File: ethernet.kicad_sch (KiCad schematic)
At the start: 38 parts

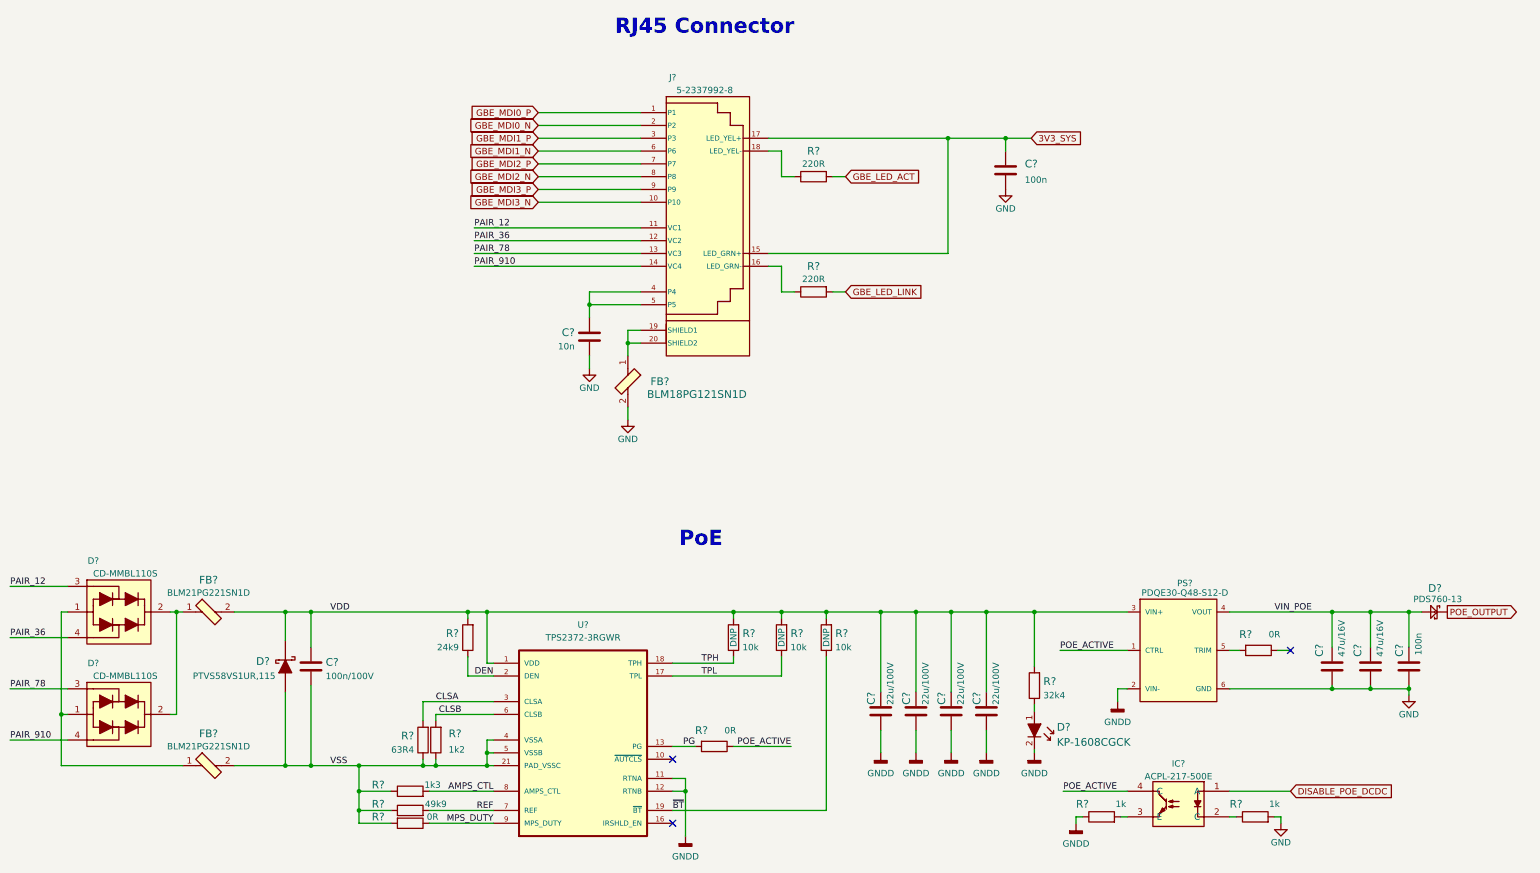
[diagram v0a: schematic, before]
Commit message: Added soft power button and annotated schematic
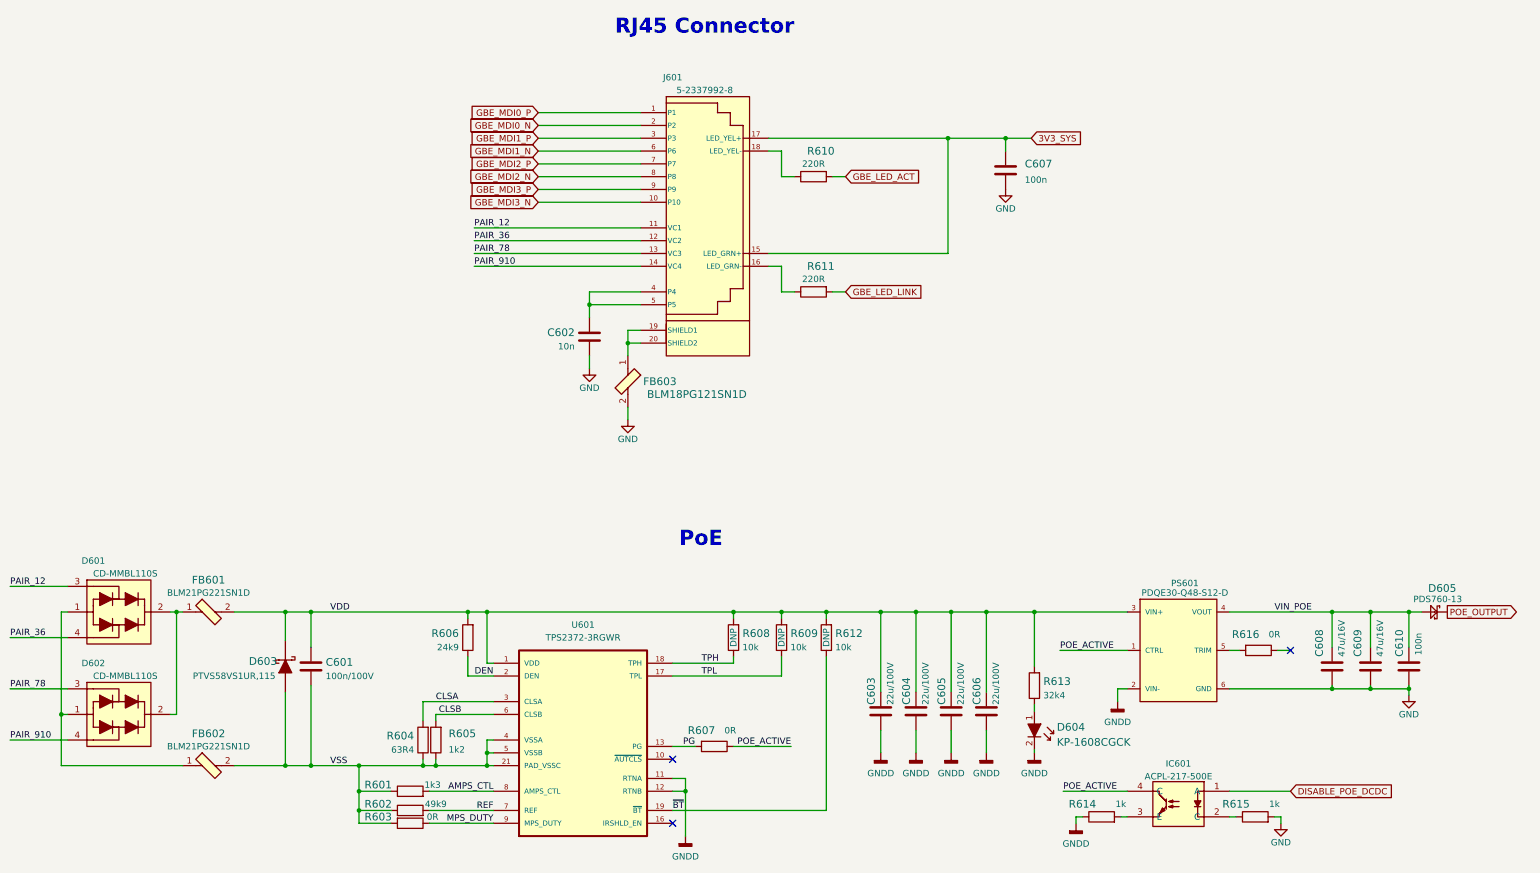
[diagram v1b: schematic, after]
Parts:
- gave numbers to parts that had none: 38

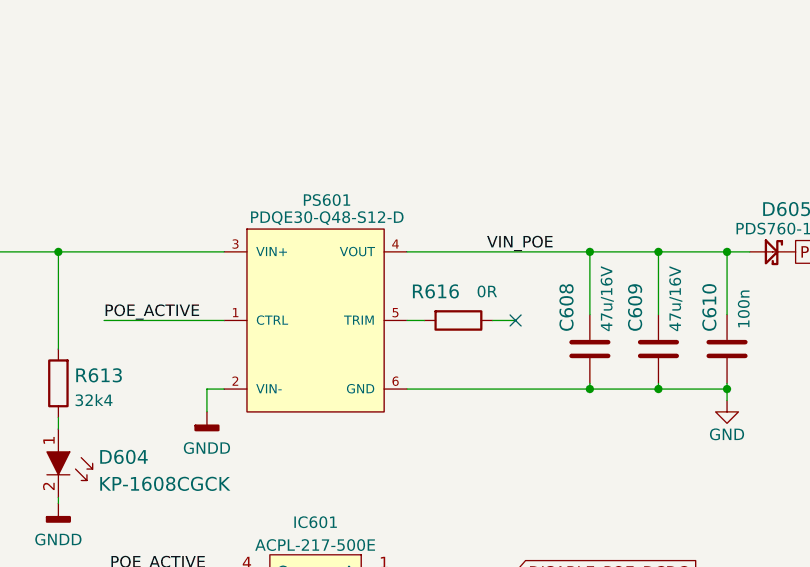
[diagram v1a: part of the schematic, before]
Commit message: Change PoE isolated DCDC to ULS-12/5-D48N-C
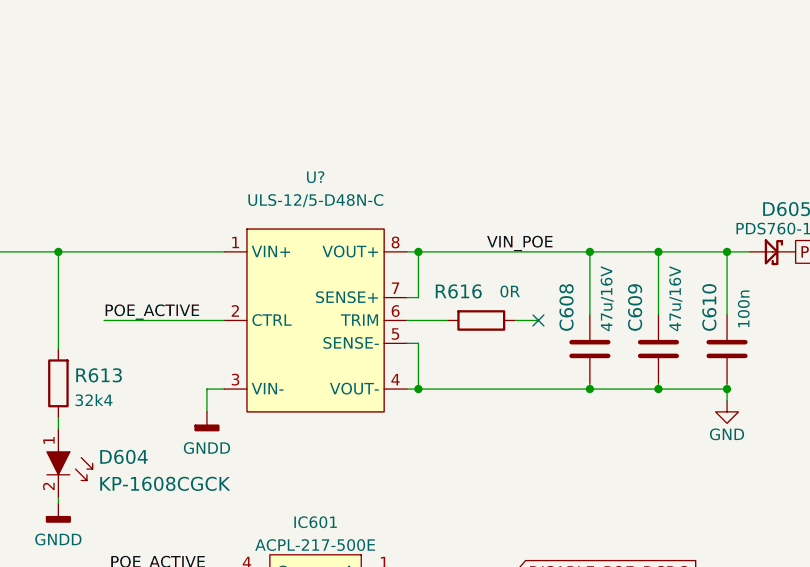
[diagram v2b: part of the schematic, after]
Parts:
- removed PS601: PDQE30-Q48-S12-D, antmicro-footprints:PDQE30-Q48, symbol antmicroDCDCConverters:PDQE30-Q48-S12-D
- added U?: ULS-12/5-D48N-C, antmicro-footprints:ULS-12_5-D48N-C, symbol antmicroDCDCConverters:ULS-12{brace}slash}5-D48N-C
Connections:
- net GND: now also U?.4 (VOUT-), U?.5 (SENSE-)
- net GNDD: now also U?.3 (VIN-)
- net POE_ACTIVE: now also U?.2 (CTRL)
- net VDD: now also U?.1 (VIN+)
- net VIN_POE: now also U?.7 (SENSE+), U?.8 (VOUT+)
- net at R616.2: now also U?.6 (TRIM)
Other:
- moved on the sheet: R616
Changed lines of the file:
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@@
   (junction (at 210.82 177.8) (diameter 0) (color 0 0 0 0)
   )
+  (junction (at 300.99 193.04) (diameter 0) (color 0 0 0 0)
+  )
   (junction (at 112.395 208.28) (diameter 0) (color 0 0 0 0)
   )
@@
   (junction (at 67.945 198.12) (diameter 0) (color 0 0 0 0)
   )
+  (junction (at 300.99 177.8) (diameter 0) (color 0 0 0 0)
+  )
   (junction (at 255.27 83.82) (diameter 0) (color 0 0 0 0)
   )
@@
   (no_connect (at 189.23 207.01))
   (no_connect (at 189.23 219.71))
-  (no_connect (at 311.785 185.42))
+  (no_connect (at 314.325 185.42))
   (wire (pts (xy 208.28 83.82) (xy 243.84 83.82))
     (stroke (width 0) (type default) (color 0 0 0 0))
   )
+  (wire (pts (xy 300.99 187.96) (xy 300.99 193.04))
+    (stroke (width 0) (type default) (color 0 0 0 0))
+  )
   (wire (pts (xy 210.82 86.36) (xy 208.28 86.36))
     (stroke (width 0) (type default) (color 0 0 0 0))
@@
     (stroke (width 0) (type default) (color 0 0 0 0))
   )
-  (wire (pts (xy 299.72 177.8) (xy 320.04 177.8))
+  (wire (pts (xy 299.72 177.8) (xy 300.99 177.8))
     (stroke (width 0) (type default) (color 0 0 0 0))
   )
@@
     (stroke (width 0) (type default) (color 0 0 0 0))
   )
+  (wire (pts (xy 299.72 182.88) (xy 300.99 182.88))
+    (stroke (width 0) (type default) (color 0 0 0 0))
+  )
   (wire (pts (xy 67.945 198.12) (xy 67.945 208.28))
     (stroke (width 0) (type default) (color 0 0 0 0))
@@
     (stroke (width 0) (type default) (color 0 0 0 0))
   )
+  (wire (pts (xy 300.99 182.88) (xy 300.99 177.8))
+    (stroke (width 0) (type default) (color 0 0 0 0))
+  )
   (wire (pts (xy 237.49 205.74) (xy 237.49 201.295))
     (stroke (width 0) (type default) (color 0 0 0 0))
@@
     (stroke (width 0) (type default) (color 0 0 0 0))
   )
+  (wire (pts (xy 300.99 193.04) (xy 320.04 193.04))
+    (stroke (width 0) (type default) (color 0 0 0 0))
+  )
   (wire (pts (xy 148.59 177.8) (xy 148.59 179.07))
     (stroke (width 0) (type default) (color 0 0 0 0))
@@
     (stroke (width 0) (type default) (color 0 0 0 0))
   )
-  (wire (pts (xy 299.72 193.04) (xy 320.04 193.04))
+  (wire (pts (xy 299.72 193.04) (xy 300.99 193.04))
     (stroke (width 0) (type default) (color 0 0 0 0))
   )
@@
     (stroke (width 0) (type default) (color 0 0 0 0))
   )
+  (wire (pts (xy 300.99 177.8) (xy 320.04 177.8))
+    (stroke (width 0) (type default) (color 0 0 0 0))
+  )
   (wire (pts (xy 277.495 193.04) (xy 279.4 193.04))
     (stroke (width 0) (type default) (color 0 0 0 0))
@@
     (stroke (width 0) (type default) (color 0 0 0 0))
   )
-  (wire (pts (xy 309.245 185.42) (xy 311.785 185.42))
+  (wire (pts (xy 311.785 185.42) (xy 314.325 185.42))
     (stroke (width 0) (type default) (color 0 0 0 0))
   )
@@
     (stroke (width 0) (type default) (color 0 0 0 0))
   )
-  (wire (pts (xy 299.72 185.42) (xy 301.625 185.42))
+  (wire (pts (xy 299.72 185.42) (xy 304.165 185.42))
     (stroke (width 0) (type default) (color 0 0 0 0))
   )
@@
     (stroke (width 0) (type default) (color 0 0 0 0))
   )
+  (wire (pts (xy 299.72 187.96) (xy 300.99 187.96))
+    (stroke (width 0) (type default) (color 0 0 0 0))
+  )
   (wire (pts (xy 266.065 185.42) (xy 279.4 185.42))
     (stroke (width 0) (type default) (color 0 0 0 0))
@@
     (pin "2")
   )
+  (symbol (lib_id "antmicroDCDCConverters:ULS-12{brace}slash}5-D48N-C") (at 289.56 185.42 0) (unit 1)
+    (in_bom yes) (on_board yes) (fields_autoplaced)
+    (property "Reference" "U?" (id 0) (at 289.56 169.545 0))
+    (property "Value" "ULS-12{slash}5-D48N-C" (id 1) (at 289.56 172.085 0))
+    (property "Footprint" "antmicro-footprints:ULS-12_5-D48N-C" (id 2) (at 289.56 172.72 0)
+      (effects (font (size 1.27 1.27)) hide)
+    )
+    (property "Datasheet" "https://www.murata.com/products/productdata/8807040286750/uls.pdf?1649388617000" (id 3) (at 289.56 198.12 0)
+      (effects (font (size 1.27 1.27)) hide)
+    )
+    (property "Manufacturer" "Murata" (id 4) (at 289.56 203.2 0)
+      (effects (font (size 1.27 1.27)) hide)
+    )
+    (property "MPN" "ULS-12/5-D48N-C" (id 5) (at 289.56 200.66 0)
+      (effects (font (size 1.27 1.27)) hide)
+    )
+    (pin "1")
+    (pin "2")
+    (pin "3")
+    (pin "4")
+    (pin "5")
+    (pin "6")
+    (pin "7")
+    (pin "8")
+  )
   (symbol (lib_id "power:GNDD") (at 191.77 222.25 0) (unit 1)
     (in_bom yes) (on_board yes) (fields_autoplaced)
@@
     (pin "2")
   )
-  (symbol (lib_id "antmicroDCDCConverters:PDQE30-Q48-S12-D") (at 289.56 185.42 0) (unit 1)
-    (in_bom yes) (on_board yes)
-    (property "Reference" "PS601" (id 0) (at 290.83 172.085 0))
-    (property "Value" "PDQE30-Q48-S12-D" (id 1) (at 290.83 173.99 0))
-    (property "Footprint" "antmicro-footprints:PDQE30-Q48" (id 2) (at 289.56 185.42 0)
-      (effects (font (size 1.27 1.27)) (justify left bottom) hide)
-    )
-    (property "Datasheet" "https://www.cui.com/product/resource/pdqe30-d.pdf" (id 3) (at 289.56 185.42 0)
-      (effects (font (size 1.27 1.27)) (justify left bottom) hide)
-    )
-    (property "STANDARD" "Manufacturer Recommendations" (id 4) (at 289.56 185.42 0)
-      (effects (font (size 1.27 1.27)) (justify left bottom) hide)
-    )
-    (property "MPN" "PDQE30-Q48-S12-D" (id 5) (at 289.56 185.42 0)
-      (effects (font (size 1.27 1.27)) (justify left bottom) hide)
-    )
-    (property "Manufacturer" "CUI" (id 6) (at 289.56 185.42 0)
-      (effects (font (size 1.27 1.27)) (justify left bottom) hide)
-    )
-    (pin "1")
-    (pin "2")
-    (pin "3")
-    (pin "4")
-    (pin "5")
-    (pin "6")
-  )
   (symbol (lib_id "antmicroModularConnectorsJacksWithMagnetics:5-2337992-8") (at 195.58 99.06 0) (unit 1)
     (in_bom yes) (on_board yes) (fields_autoplaced)
@@
     (pin "9")
   )
-  (symbol (lib_id "antmicroResistors0603:R_0R_0603") (at 305.435 185.42 180) (unit 1)
+  (symbol (lib_id "antmicroResistors0603:R_0R_0603") (at 307.975 185.42 180) (unit 1)
     (in_bom yes) (on_board yes)
-    (property "Reference" "R616" (id 0) (at 302.895 182.245 0)
+    (property "Reference" "R616" (id 0) (at 305.435 182.245 0)
       (effects (font (size 1.524 1.524)))
     )
-    (property "Value" "R_0R_0603" (id 1) (at 305.435 181.61 0)
+    (property "Value" "R_0R_0603" (id 1) (at 307.975 181.61 0)
       (effects (font (size 1.524 1.524)) hide)
     )
-    (property "Footprint" "antmicro-footprints:0603-res" (id 2) (at 300.355 190.5 0)
+    (property "Footprint" "antmicro-footprints:0603-res" (id 2) (at 302.895 190.5 0)
       (effects (font (size 1.524 1.524)) (justify left) hide)
     )
-    (property "Datasheet" "" (id 3) (at 305.435 185.42 0)
+    (property "Datasheet" "" (id 3) (at 307.975 185.42 0)
       (effects (font (size 1.27 1.27)) hide)
     )
-    (property "Manufacturer" "BOURNS" (id 4) (at 300.355 195.58 0)
+    (property "Manufacturer" "BOURNS" (id 4) (at 302.895 195.58 0)
       (effects (font (size 1.524 1.524)) (justify left) hide)
     )
-    (property "MPN" "CR0603-J/-000ELF" (id 5) (at 300.355 193.04 0)
+    (property "MPN" "CR0603-J/-000ELF" (id 5) (at 302.895 193.04 0)
       (effects (font (size 1.524 1.524)) (justify left) hide)
     )
-    (property "Val" "0R" (id 6) (at 308.61 182.245 0))
+    (property "Val" "0R" (id 6) (at 311.15 182.245 0))
     (pin "1")
     (pin "2")

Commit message: Unified schematic look of ethernet sheet, improved shielding of eth connector, replaced gnd symbols
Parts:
- removed FB603: BLM18PG121SN1D, antmicro-footprints:0603-res, symbol antmicroFerriteBeadsandChips:BLM18PG121SN1D
- added C611: C_100n_0402, antmicro-footprints:0402-cap, symbol antmicroCapacitors0402:C_100n_0402
- added R617: R_200R_0402, antmicro-footprints:0402-res, symbol antmicroResistors0402:R_200R_0402
- FB601, FB602: value BLM21PG221SN1D -> (none); footprint antmicro-footprints:0805-res -> (none)
- gave numbers to parts that had none: 1
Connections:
- net GND: now also C611.2, R617.1
- net at J601.19 (SHIELD1), J601.20 (SHIELD2): now also C611.1, R617.2
- net 3V3_SYS renamed +3V3
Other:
- note added: "ETHERNET CONNECTOR"
- note added: "POWER OVER ETHERNET"
- note removed: "PoE"
- note removed: "RJ45 Connector"
- moved on the sheet: C601, C602, C603, C604, C605, C606, C607, C608, C609, C610, D601, D602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

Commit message: Add CSI MUX labels and numbers to refer to on Block Diagram, update all GND symbols from global library
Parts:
- FB601, FB602: value (none) -> BLM21PG221SN1D; footprint (none) -> antmicro-footprints:0805-res
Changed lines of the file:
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@@
       (effects (font (size 1.524 1.524)))
     )
-    (property "Value" "" (id 1) (at 101.6 177.8 0)
-      (effects (font (size 1.27 1.27)) hide)
-    )
-    (property "Footprint" "" (id 2) (at 101.6 188.595 0)
+    (property "Value" "BLM21PG221SN1D" (id 1) (at 101.6 177.8 0)
+      (effects (font (size 1.27 1.27)) hide)
+    )
+    (property "Footprint" "antmicro-footprints:0805-res" (id 2) (at 101.6 188.595 0)
       (effects (font (size 1.524 1.524)) (justify left) hide)
     )
@@
   (symbol (lib_id "power:GND") (at 166.37 101.6 0) (unit 1)
     (in_bom yes) (on_board yes)
-    (property "Reference" "#PWR0601" (id 0) (at 166.37 107.95 0)
+    (property "Reference" "#PWR?" (id 0) (at 166.37 107.95 0)
       (effects (font (size 1.27 1.27)) hide)
     )
@@
       (effects (font (size 1.524 1.524)))
     )
-    (property "Value" "" (id 1) (at 101.6 208.28 0)
-      (effects (font (size 1.27 1.27)) hide)
-    )
-    (property "Footprint" "" (id 2) (at 101.6 219.075 0)
+    (property "Value" "BLM21PG221SN1D" (id 1) (at 101.6 208.28 0)
+      (effects (font (size 1.27 1.27)) hide)
+    )
+    (property "Footprint" "antmicro-footprints:0805-res" (id 2) (at 101.6 219.075 0)
       (effects (font (size 1.524 1.524)) (justify left) hide)
     )
@@
   (symbol (lib_id "power:GND") (at 172.72 111.76 0) (unit 1)
     (in_bom yes) (on_board yes) (fields_autoplaced)
-    (property "Reference" "#PWR0602" (id 0) (at 172.72 118.11 0)
+    (property "Reference" "#PWR?" (id 0) (at 172.72 118.11 0)
       (effects (font (size 1.27 1.27)) hide)
     )
@@
   (symbol (lib_id "power:GND") (at 257.81 66.04 0) (unit 1)
     (in_bom yes) (on_board yes) (fields_autoplaced)
-    (property "Reference" "#PWR0609" (id 0) (at 257.81 72.39 0)
+    (property "Reference" "#PWR?" (id 0) (at 257.81 72.39 0)
       (effects (font (size 1.27 1.27)) hide)
     )
@@
   (symbol (lib_id "power:GND") (at 182.88 111.76 0) (unit 1)
     (in_bom yes) (on_board yes) (fields_autoplaced)
-    (property "Reference" "#PWR0608" (id 0) (at 182.88 118.11 0)
+    (property "Reference" "#PWR?" (id 0) (at 182.88 118.11 0)
       (effects (font (size 1.27 1.27)) hide)
     )
@@
   (symbol (lib_id "power:GND") (at 339.725 198.12 0) (unit 1)
     (in_bom yes) (on_board yes) (fields_autoplaced)
-    (property "Reference" "#PWR0614" (id 0) (at 339.725 204.47 0)
+    (property "Reference" "#PWR?" (id 0) (at 339.725 204.47 0)
       (effects (font (size 1.27 1.27)) hide)
     )
@@
   (symbol (lib_id "power:GND") (at 314.325 223.52 0) (unit 1)
     (in_bom yes) (on_board yes) (fields_autoplaced)
-    (property "Reference" "#PWR0613" (id 0) (at 314.325 229.87 0)
-      (effects (font (size 1.27 1.27)) hide)
-    )
+    (property "Reference" "#PWR?" (id 0) (at 314.325 229.87 0)
+      (effects (font (size 1.27 1.27)) hide)
+    )

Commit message: SCH: Update title block, set revision to 1.0.0
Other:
- title: Jetson Orin NX Baseboard -> Jetson Orin Baseboard
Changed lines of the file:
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@@
   (paper "A3")
   (title_block
-    (title "Jetson Orin NX Baseboard")
+    (title "Jetson Orin Baseboard")
+    (rev "1.0.0")
     (company "Antmicro Ltd")
     (comment 1 "www.antmicro.com")
